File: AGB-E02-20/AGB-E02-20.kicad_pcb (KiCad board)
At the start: 2 copper layers, 51 x 31.1 mm, 11 parts, among them U0 CartBus, U1 MX23L12806-12C, U2 LE26FV10N1TS

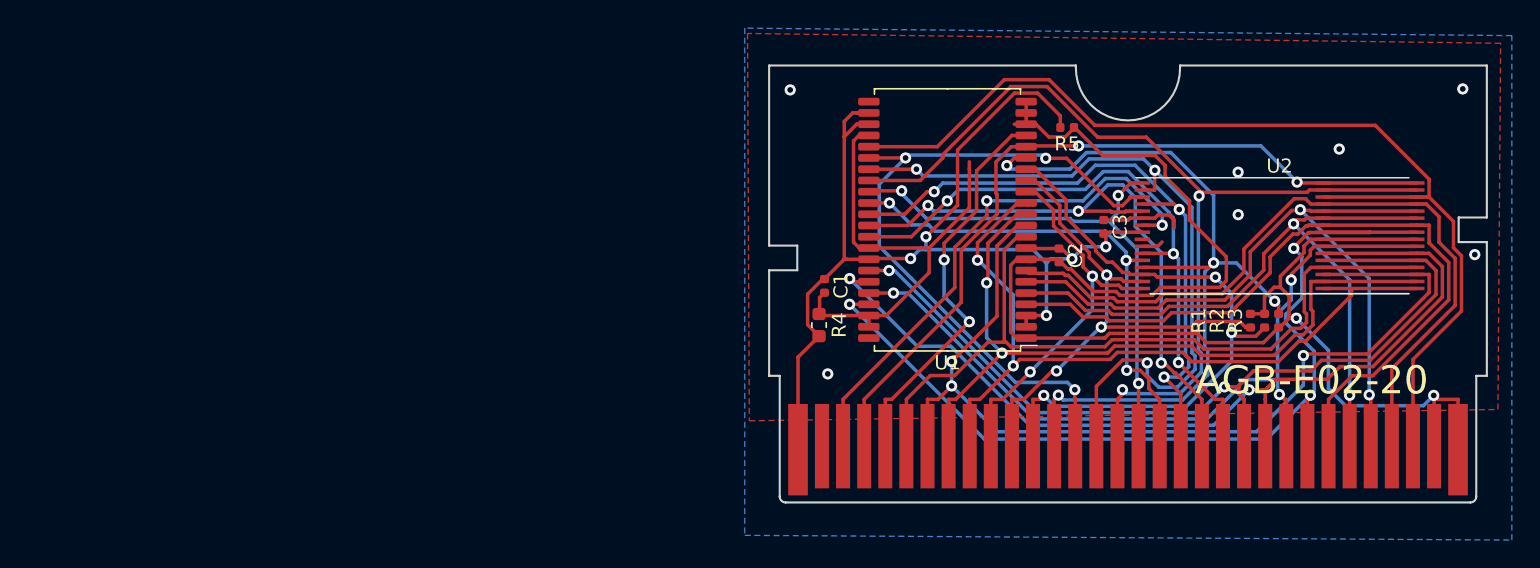
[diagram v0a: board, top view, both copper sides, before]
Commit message: Update AGB-E02-20
AGB-E02-20 looks much more "OEM" now
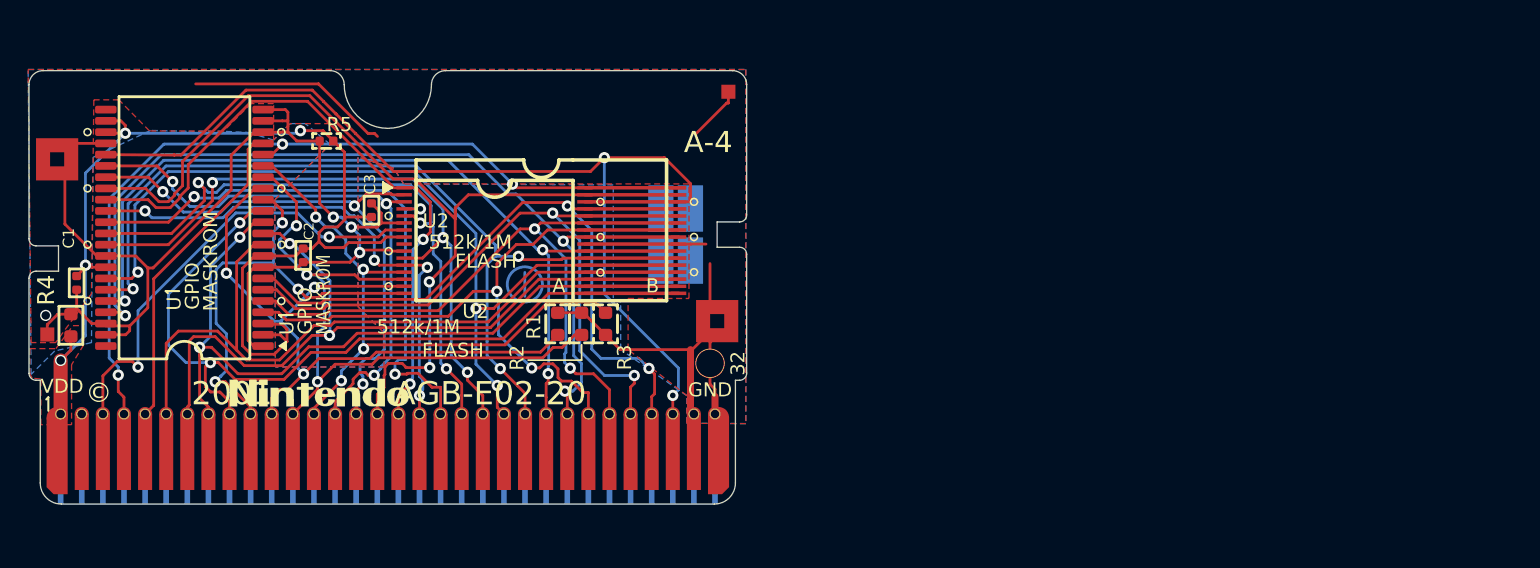
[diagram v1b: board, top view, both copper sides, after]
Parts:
- added G1: Nintendo Logo, Custom:Nintendo-GBA-Logo, F.Cu at (78.2, 115.9)
- added Pad1: MountingHole_Pad, Custom:Nintendo_3x3_GNDPad, F.Cu at (106.5, 110.8)
- added Pad2: MountingHole_Pad, Custom:Nintendo_3x3_GNDPad, F.Cu at (59.6, 99.3)
- added Pad3: MountingHole_Pad, Custom:Nintendo_1x1_Pad, F.Cu at (107.3, 94.5)
- added Pad4: MountingHole_Pad, Custom:Nintendo_1x1_Pad, F.Cu at (58.9, 111.8)
- added PlatedHole1: MountingHole, Custom:TestPoint_Plated_Hole_D2.0mm, F.Cu at (106.0, 113.8)
- added dateindicator: GBA-ProductionIndicator, Custom:GBA-ProductionIndicator, B.Cu at (103.5, 104.7)
- C1, C2, C3: footprint Capacitor_SMD:C_0402_1005Metric -> Custom:C_0402_AGB
- R1, R2, R3: footprint Resistor_SMD:R_0402_1005Metric -> Custom:R_0603_AGB
- R4: footprint Capacitor_SMD:C_0603_1608Metric -> Custom:C_0603_AGB
- R5: footprint Resistor_SMD:R_0402_1005Metric -> Custom:R_0402_AGB-Opt
- U0: footprint NintendoFootprints:CartBus -> Connector_GameBoy:GameBoy_GamePak_AGB-002_P1.50mm_Edge
- moved U1 54.2 mm to (68.6, 104.2)
- moved C2 53.7 mm to (77.0, 106.1)
- moved R4 53.2 mm to (60.5, 111.1)
- moved C1 53.1 mm to (61.0, 108.1)
- moved R5 52.6 mm to (78.7, 98.0), turned to 0 degrees
- moved U2 52.5 mm to (94.0, 105.1)
- moved C3 52.0 mm to (81.9, 102.9)
- moved R1 49.2 mm to (95.1, 111.0)
- moved R2 48.5 mm to (96.8, 111.0)
- moved R3 47.8 mm to (98.5, 111.0)
- moved U0 28.5 mm to (83.1, 114.4)
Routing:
- net A1: track 68.8 -> 54.0 mm, vias 3 -> 2
- net A7: track 58.2 -> 44.7 mm
- net A9: track 52.9 -> 40.1 mm
- net A5: track 38.8 -> 50.3 mm
- net A8: track 50.5 -> 41.3 mm
- net A11: track 39.2 -> 46.5 mm, vias 3 -> 2
- net D2: track 56.9 -> 63.8 mm
- net D4: track 53.3 -> 46.9 mm, vias 0 -> 2
- net CS: track 28.6 -> 23.1 mm, vias 2 -> 0
- net WR: track 38.0 -> 32.8 mm
- net RD: track 55.6 -> 60.8 mm, vias 2 -> 3
- net A4: track 27.8 -> 32.8 mm, vias 2 -> 3
- net A13: track 46.5 -> 43.0 mm
- net A6: track 45.9 -> 49.0 mm
- net CS2: track 73.6 -> 76.4 mm, vias 0 -> 2
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- added copper zone on F.Cu, net +3V3
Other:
- board size 51 x 31.1 mm -> 51 x 30.8 mm
- net class Default: trace_width 0.25 -> 0.2; via_drill 0.4 -> 0.55
- board text added: "2001 AGB-E02-20"
- board text added: "512k/1M"
- board text added: "A-4"
- board text added: "FLASH"
- board text added: "GND"
- board text added: "GPIO"
- board text added: "MASKROM"
- board text added: "U"
- board text added: "U2"
- board text added: "VDD"
- board text added: "©"
- board text removed: "AGB-E02-20"
- board text removed: "V1.0"

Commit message: Update AGB-E02-20
AGB-E02-20 is now mostly identical to the original pcb (this was a lot of work)
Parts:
- C1, C2, C3: value C -> 100nF - 0402
- R4: value Cap -> 2.2uF - 0603
